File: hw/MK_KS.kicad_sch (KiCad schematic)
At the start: 40 parts, among them J10 Screw_Terminal_01x02, J11 TRS-JACK-KP, J3 KEY_SND_IF, J8 Conn_Coaxial_Power, J9 Screw_Terminal_01x02, Q1 G01N20LE, U4 LM393ADR, U5 Sounder

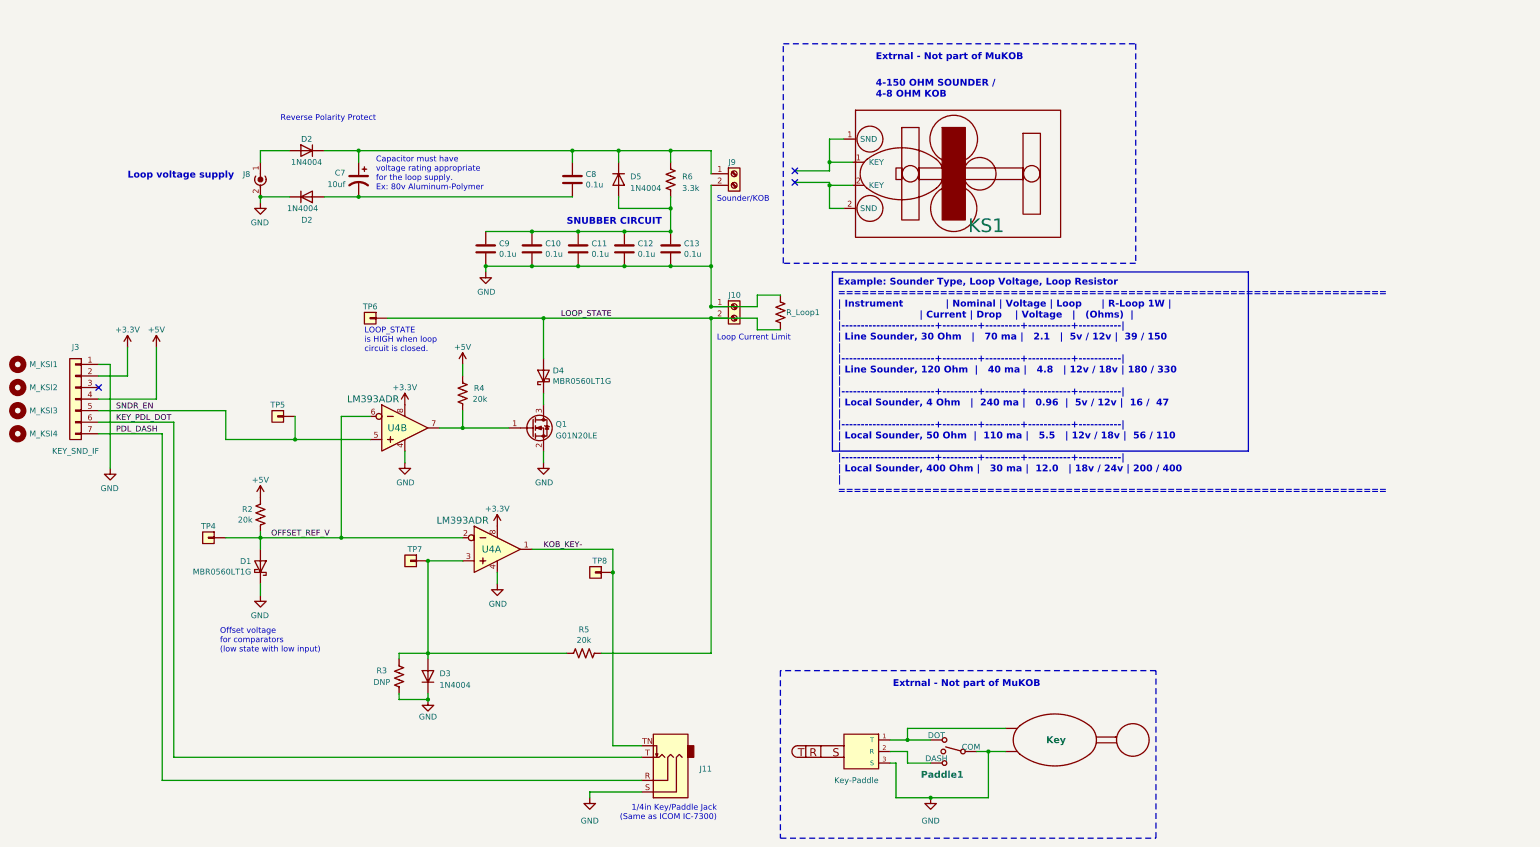
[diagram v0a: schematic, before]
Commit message: Reorganize onto 3 boards. Use 20pin UI connector.
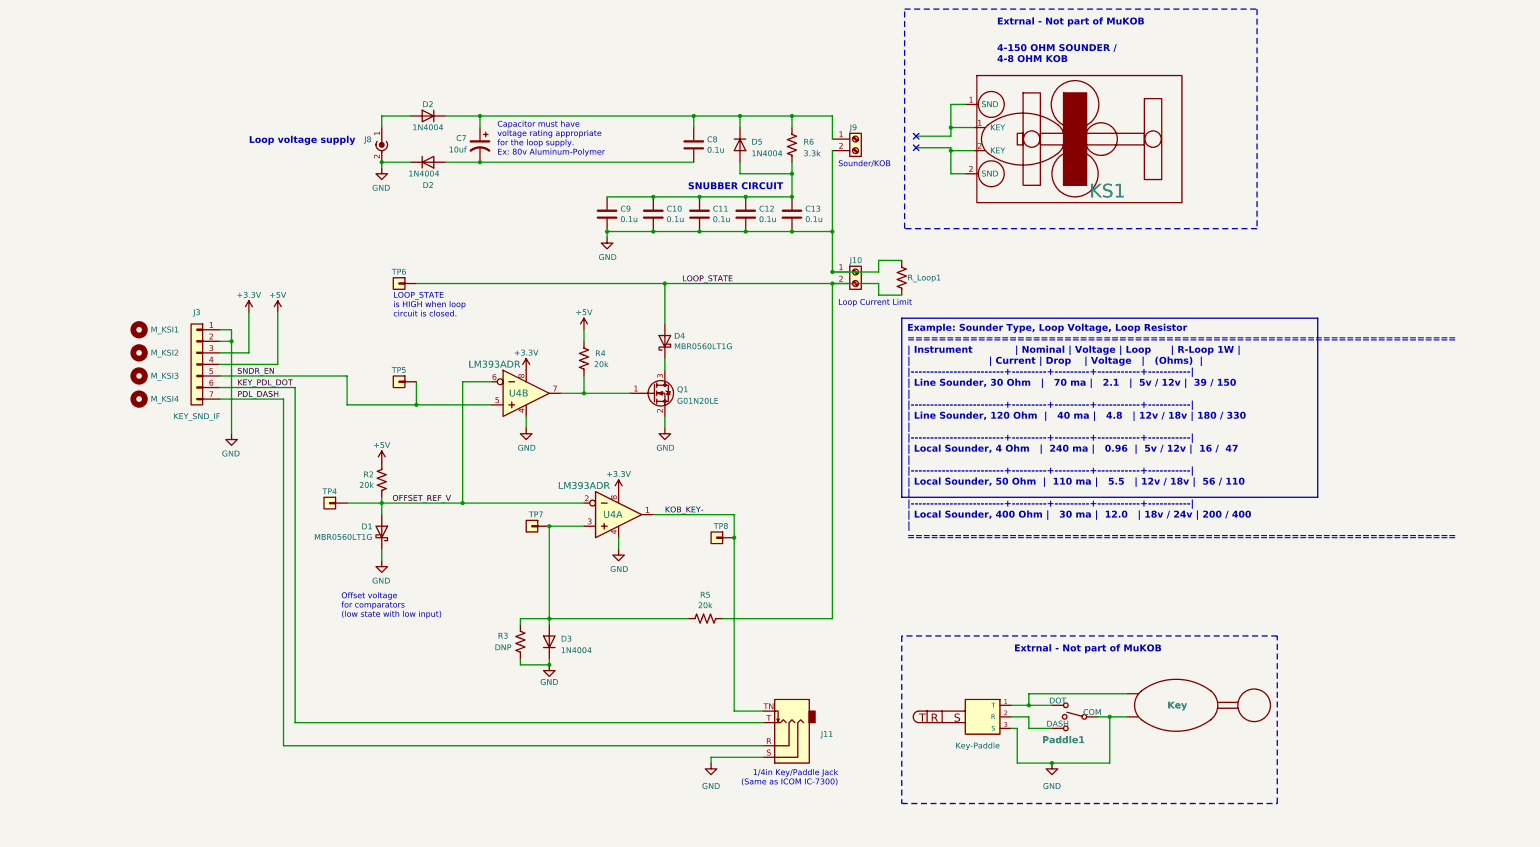
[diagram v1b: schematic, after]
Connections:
- net +3.3V: now also J3.3 (Pin_3); no longer J3.2 (Pin_2)
- net GND: now also J3.2 (Pin_2)
- no-connect marks 3 -> 2
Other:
- note removed: "Reverse Polarity Protect"
- moved on the sheet: C10, C11, C12, C13, C7, C8, C9, D1, D2, D3, D4, D5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

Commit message: Electrical checks complete.
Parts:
- removed M_KSI1, M_KSI2, M_KSI3, M_KSI4: MountingHole, MountingHole:MountingHole_2.7mm_M2.5, symbol Mechanical:MountingHole
- added C9 (x2): 1uF, Capacitor_SMD:C_1206_3216Metric_Pad1.33x1.80mm_HandSolder, symbol Device:C
- added D1: MBR0560LT1G, Diode_SMD:D_SOD-123, symbol Diode:MBR0560
- added D7: 1N4148W, Diode_SMD:D_SOD-123, symbol Diode:1N4148W
- added J4: MKOB-Serial, symbol Connector:DE9_Receptacle_MountingHoles
- added J5: USB_OTG, symbol Connector:USB_OTG
- added JP1, JP2: 1x2 Header, symbol Jumper:Jumper_2_Open
- added LED1: SNDR, LED_THT:LED_D5.0mm, symbol Device:LED
- added M_KSI1, M_KSI2, M_KSI3, M_KSI4, SHLD-1, SHLD-2, SHLD-3, SHLD-4: MountingHole_Pad, symbol Mechanical:MountingHole_Pad
- added Q1 (x2): 2N3904, Package_TO_SOT_THT:TO-92_Inline, symbol Transistor_BJT:2N3904
- added Q8: 2N3905, Package_TO_SOT_THT:TO-92_Inline, symbol Transistor_BJT:2N3905
- added R2: 1k, Resistor_SMD:R_1206_3216Metric_Pad1.30x1.75mm_HandSolder, symbol Device:R_US
- added R2: 100, Resistor_SMD:R_1206_3216Metric_Pad1.30x1.75mm_HandSolder, symbol Device:R_US
- added R5: 10k, Resistor_SMD:R_1206_3216Metric_Pad1.30x1.75mm_HandSolder, symbol Device:R_US
- added R6: 1k, Resistor_THT:R_Axial_DIN0207_L6.3mm_D2.5mm_P10.16mm_Horizontal, symbol Device:R_Small_US
- added R7: 270, Resistor_THT:R_Axial_DIN0207_L6.3mm_D2.5mm_P10.16mm_Horizontal, symbol Device:R_Small_US
- added SW1: KEY/DOT-SW, Button_Switch_SMD:SW_Push_1P1T_NO_Vertical_Wuerth_434133025816, symbol Switch:SW_Push
- added SW1: CLOSER-SW, symbol Switch:SW_SPST
- added SW1: DASH-SW, Button_Switch_SMD:SW_Push_1P1T_NO_Vertical_Wuerth_434133025816, symbol Switch:SW_Push
- added U2: LM358, symbol Amplifier_Operational:LM358
- added U3: MCP1702T-3302E, Package_TO_SOT_SMD:SOT-23, symbol Regulator_Linear:MCP1700x-330xxTT
- D2, D3, D5: footprint Diode_SMD:D_SMB_Handsoldering -> Diode_THT:D_DO-41_SOD81_P10.16mm_Horizontal
- R_Loop1: now left out of the parts list
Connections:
- net +3.3V: now also JP1.2 (B), Q8.1 (E), R6.1
- net +5V: now also C9.1, D1.1 (K), JP2.1 (A), R2.1, U3.3 (VI)
- net GND: now also C7.2, C8.2, D2.2 (A), C9.2, C9.2, D7.2 (A), J4.0 (PAD), J4.5, J5.5 (GND), J5.6 (Shield), M_KSI1.1, M_KSI2.1, M_KSI3.1, M_KSI4.1, Q1.1 (E), R7.2, SHLD-1.1, SHLD-2.1, SHLD-3.1, SHLD-4.1, SW1.1, SW1.1, SW1.1 (A), U3.1 (GND); no longer D2.1 (K), J8.2 (Ext), R_Loop1.1
- net KEY_PDL_DOT: now also SW1.2, SW1.2 (B), U2.3 (+)
- net LOOP_STATE: no longer R_Loop1.2
- net OFFSET_REF_V: now also U2.2 (-), U2.6 (-)
- net PDL_DASH: now also SW1.2, U2.5 (+)
- net SNDR_EN: now also Q8.3 (C), R2.1
- net at C7.1, C8.1, D2.1 (K)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: now also JP2.2 (B)
- new net: D2.1 (K), J8.2 (Ext)
- new net: Q1.1 (E), R7.1
- new net: Q1.3 (C), Q8.2 (B), R6.2
- new net: C9.1, JP1.1 (A), U3.2 (VO)
- new net: LED1.1 (K), Q1.3 (C)
- new net: LED1.2 (A), R2.2
- new net: D1.2 (A), J5.1 (VBUS)
- new net: Q1.2 (B), R2.2
- new net CTS: J4.8, U2.7
- new net DCD: J4.1
- new net DSR: J4.6, U2.1
- new net DTR: J4.4, U2.8 (V+)
- new net LOOP_ENGZ: D7.1 (K), Q1.2 (B), R5.1
- new net RI: J4.9
- new net RTS: J4.7, R5.2
- new net RXD: J4.2
- new net TXD: J4.3, U2.4 (V-)
- no-connect marks 2 -> 8
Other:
- note added: "For Metal Shield"
- note added: "KOB Debug Power DO NOT CONNECT w/Loop Powered"
- note added: "Key/Paddle - Sounder DEBUG Insert 'dummy' in J2 to use dot/dash"
- note added: "MorseKOB/MKOB Interface (optional) DO NOT CONNECT J3 WHEN IN USE"
- note added: "MorseKOB/MKOB Interface Power DO NOT CONNECT for MuKOB"
- note added: "USB Power for MorseKOB/MKOB Interface DO NOT USE for MuKOB"
- moved on the sheet: C10, C11, C12, C13, C7, C8, C9, D1, D2, D3, D4, D5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

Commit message: KeySounder schematic ready for PCB layout.
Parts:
- removed JP2: 1x2 Header, symbol Jumper:Jumper_2_Open
- added JP1: Conn_01x02, symbol Connector_Generic:Conn_01x02
- added OP6: OP_A-B, Connector_PinHeader_1.00mm:PinHeader_1x03_P1.00mm_Vertical, symbol MuKOB:Option_A-B
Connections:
- net +5V: now also JP1.1 (Pin_1), OP6.1 (A); no longer C9.1, U3.3 (VI)
- net LOOP_PWR: now reaches C7.1, C8.1, D2.1 (K), D5.1 (K), J9.1 (Pin_1), R6.1
- net LOOP_PWR: now also JP1.2 (Pin_2), OP6.3 (B)
- new net: C9.1, OP6.2 (C), U3.3 (VI)
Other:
- moved on the sheet: D1, J5

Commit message: Schematic updates. Reorg components between boards. 20 pin ribbon.
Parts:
- removed J-SP1: Key-Paddle, symbol Audio-Plug-TRS:SP-TRS
- removed J11: TRS-JACK-KP, symbol Connector_Audio:AudioJack3_SwitchT
- removed KEY-EXT1: Key, symbol rpikobhat-rescue:Key-Telegraph
- removed Paddle1: PDL_EXT, symbol Switch:SW_SPDT_MSM
- added JP2: 1x2 Header, Connector_PinHeader_2.54mm:PinHeader_1x02_P2.54mm_Vertical, symbol Jumper:Jumper_2_Open
- J3: renamed from J4; footprint (none) -> Connector_Dsub:DSUB-9_Female_Horizontal_P2.77x2.84mm_EdgePinOffset9.90mm_Housed_MountingHolesOffset11.32mm
- J4: renamed from J3; footprint (none) -> Connector_PinSocket_2.54mm:PinSocket_1x07_P2.54mm_Vertical
- JP1: footprint (none) -> Connector_PinHeader_2.54mm:PinHeader_1x02_P2.54mm_Vertical
- JP1: value Conn_01x02 -> LoopDbgPwr; footprint (none) -> Connector_PinHeader_2.54mm:PinHeader_1x02_P2.54mm_Vertical
- OP6: value OP_A-B -> 5V-SRC; footprint Connector_PinHeader_1.00mm:PinHeader_1x03_P1.00mm_Vertical -> Connector_PinHeader_2.54mm:PinHeader_1x03_P2.54mm_Vertical
- TP4, TP5, TP6, TP7, TP8: footprint (none) -> Connector_PinHeader_2.54mm:PinHeader_1x01_P2.54mm_Vertical
- renumbered D7 to D8, J5 to J1, U3 to U1, U2 to U3
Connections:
- net KOB_KEY-: now also JP2.2 (B)
- net KEY_PDL_DOT renamed KEY-
- net KEY-: now also JP2.1 (A)
- net PDL_DASH renamed PDL_DASH-
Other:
- note added: "Key/Paddle - Sounder DEBUG Remove JP2 to use."
- note added: "Normally connected. Remove to use the 'Test Key/Closer'"
- note removed: "1/4in Key/Paddle Jack (Same as ICOM IC-7300)"
- note removed: "Key/Paddle - Sounder DEBUG Insert 'dummy' in J2 to use dot/dash"

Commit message: UI PCB initial
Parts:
- D2, D3, D5: value 1N4004 -> 1N4148; footprint Diode_THT:D_DO-41_SOD81_P10.16mm_Horizontal -> Diode_SMD:D_SOD-123
- D6: renamed from D8; value 1N4148W -> 1N4148
- J1: footprint (none) -> AES_Library:USB_Micro-B_Amphenol_10103594-0001LF_Horizontal_modified
- M_KSI1, M_KSI2, M_KSI3, M_KSI4: footprint (none) -> MountingHole:MountingHole_3.2mm_M3_ISO7380
- SHLD-1, SHLD-2, SHLD-3, SHLD-4: footprint (none) -> MountingHole:MountingHole_4.3mm_M4_ISO14580_Pad_TopBottom
- SW1: footprint (none) -> AES_Library:SW-TGL-Micro-DPST-CIT
- U3: footprint (none) -> Package_SO:SOIC-8_3.9x4.9mm_P1.27mm
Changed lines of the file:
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@@
       (project "MK_KS"
         (path "/c58d90c2-85f3-4e69-91d5-1bcb030f2211"
-          (reference "D6") (unit 1)
+          (reference "D8") (unit 1)
         )
       )
@@
       (effects (font (size 1.27 1.27)) (justify left))
     )
-    (property "Footprint" "" (at 73.66 213.36 0)
+    (property "Footprint" "AES_Library:SW-TGL-Micro-DPST-CIT" (at 73.66 213.36 0)
       (effects (font (size 1.27 1.27)) hide)
     )
@@
       (effects (font (size 1.27 1.27)) (justify left) hide)
     )
-    (property "Footprint" "" (at 400.05 213.36 0)
+    (property "Footprint" "MountingHole:MountingHole_4.3mm_M4_ISO14580_Pad_TopBottom" (at 400.05 213.36 0)
       (effects (font (size 1.27 1.27)) hide)
     )
@@
       (effects (font (size 1.27 1.27)))
     )
-    (property "Footprint" "" (at 36.83 49.53 0)
+    (property "Footprint" "AES_Library:USB_Micro-B_Amphenol_10103594-0001LF_Horizontal_modified" (at 36.83 49.53 0)
       (effects (font (size 1.27 1.27)) hide)
     )
@@
       (effects (font (size 1.27 1.27)) (justify left) hide)
     )
-    (property "Footprint" "" (at 29.21 163.83 0)
+    (property "Footprint" "MountingHole:MountingHole_3.2mm_M3_ISO7380" (at 29.21 163.83 0)
       (effects (font (size 1.27 1.27)) hide)
     )
@@
       (effects (font (size 1.27 1.27)) (justify left) hide)
     )
-    (property "Footprint" "" (at 400.05 208.28 0)
+    (property "Footprint" "MountingHole:MountingHole_4.3mm_M4_ISO14580_Pad_TopBottom" (at 400.05 208.28 0)
       (effects (font (size 1.27 1.27)) hide)
     )
@@
       (effects (font (size 1.27 1.27)) (justify left) hide)
     )
-    (property "Footprint" "" (at 29.21 173.99 0)
+    (property "Footprint" "MountingHole:MountingHole_3.2mm_M3_ISO7380" (at 29.21 173.99 0)
       (effects (font (size 1.27 1.27)) hide)
     )
@@
   (symbol (lib_id "Diode:1N4148W") (at 86.36 109.22 270) (unit 1)
     (in_bom yes) (on_board yes) (dnp no)
-    (property "Reference" "D8" (at 81.28 106.68 90)
-      (effects (font (size 1.27 1.27)) (justify left))
-    )
-    (property "Value" "1N4148W" (at 74.93 109.22 90)
+    (property "Reference" "D6" (at 81.28 106.68 90)
+      (effects (font (size 1.27 1.27)) (justify left))
+    )
+    (property "Value" "1N4148" (at 74.93 109.22 90)
       (effects (font (size 1.27 1.27)) (justify left))
     )
@@
       (project "MK_KS"
         (path "/c58d90c2-85f3-4e69-91d5-1bcb030f2211"
-          (reference "D8") (unit 1)
+          (reference "D6") (unit 1)
         )
       )
@@
       (effects (font (size 1.27 1.27)) (justify right))
     )
-    (property "Value" "1N4004" (at 151.13 67.31 0)
+    (property "Value" "1N4148" (at 151.13 67.31 0)
       (effects (font (size 1.27 1.27)) (justify right))
     )
-    (property "Footprint" "Diode_THT:D_DO-41_SOD81_P10.16mm_Horizontal" (at 148.59 60.325 0)
+    (property "Footprint" "Diode_SMD:D_SOD-123" (at 148.59 60.325 0)
       (effects (font (size 1.27 1.27)) hide)
     )
@@
       (effects (font (size 1.27 1.27)) (justify left) hide)
     )
-    (property "Footprint" "" (at 400.05 218.44 0)
+    (property "Footprint" "MountingHole:MountingHole_4.3mm_M4_ISO14580_Pad_TopBottom" (at 400.05 218.44 0)
       (effects (font (size 1.27 1.27)) hide)
     )
@@
       (effects (font (size 1.27 1.27)) (justify left) hide)
     )
-    (property "Footprint" "" (at 29.21 179.07 0)
+    (property "Footprint" "MountingHole:MountingHole_3.2mm_M3_ISO7380" (at 29.21 179.07 0)
       (effects (font (size 1.27 1.27)) hide)
     )
@@
       (effects (font (size 1.27 1.27)))
     )
-    (property "Value" "1N4004" (at 148.59 57.15 0)
-      (effects (font (size 1.27 1.27)))
-    )
-    (property "Footprint" "Diode_THT:D_DO-41_SOD81_P10.16mm_Horizontal" (at 148.59 59.055 0)
+    (property "Value" "1N4148" (at 148.59 57.15 0)
+      (effects (font (size 1.27 1.27)))
+    )
+    (property "Footprint" "Diode_SMD:D_SOD-123" (at 148.59 59.055 0)
       (effects (font (size 1.27 1.27)) hide)
     )
@@
       (effects (font (size 1.27 1.27)))
     )
-    (property "Footprint" "" (at 80.01 142.24 0)
+    (property "Footprint" "Package_SO:SOIC-8_3.9x4.9mm_P1.27mm" (at 80.01 142.24 0)
       (effects (font (size 1.27 1.27)) hide)
     )
@@
       (effects (font (size 1.27 1.27)) (justify left) hide)
     )
-    (property "Footprint" "" (at 29.21 168.91 0)
+    (property "Footprint" "MountingHole:MountingHole_3.2mm_M3_ISO7380" (at 29.21 168.91 0)
       (effects (font (size 1.27 1.27)) hide)
     )
@@
       (effects (font (size 1.27 1.27)) (justify right) hide)
     )
-    (property "Footprint" "" (at 76.2 74.93 0)
+    (property "Footprint" "Package_SO:SOIC-8_3.9x4.9mm_P1.27mm" (at 76.2 74.93 0)
       (effects (font (size 1.27 1.27)) hide)
     )
@@
       (effects (font (size 1.27 1.27)) (justify right))
     )
-    (property "Value" "1N4004" (at 170.18 227.965 90)
+    (property "Value" "1N4148" (at 170.18 227.965 90)
       (effects (font (size 1.27 1.27)) (justify right))
     )
-    (property "Footprint" "Diode_THT:D_DO-41_SOD81_P10.16mm_Horizontal" (at 172.085 226.06 0)
+    (property "Footprint" "Diode_SMD:D_SOD-123" (at 172.085 226.06 0)
       (effects (font (size 1.27 1.27)) hide)
     )
@@
       (effects (font (size 1.27 1.27)) (justify left) hide)
     )
-    (property "Footprint" "" (at 400.05 223.52 0)
+    (property "Footprint" "MountingHole:MountingHole_4.3mm_M4_ISO14580_Pad_TopBottom" (at 400.05 223.52 0)
       (effects (font (size 1.27 1.27)) hide)
     )
@@
       (effects (font (size 1.27 1.27)))
     )
-    (property "Footprint" "" (at 76.2 74.93 0)
+    (property "Footprint" "Package_SO:SOIC-8_3.9x4.9mm_P1.27mm" (at 76.2 74.93 0)
       (effects (font (size 1.27 1.27)) hide)
     )
@@
       (effects (font (size 1.27 1.27)) (justify left))
     )
-    (property "Value" "1N4004" (at 209.55 62.865 90)
-      (effects (font (size 1.27 1.27)) (justify left))
-    )
-    (property "Footprint" "Diode_THT:D_DO-41_SOD81_P10.16mm_Horizontal" (at 202.565 60.96 0)
-      (effects (font (size 1.27 1.27)) hide)
-    )
+    (property "Value" "1N4148" (at 209.55 62.865 90)
+      (effects (font (size 1.27 1.27)) (justify left))
+    )
+    (property "Footprint" "Diode_SMD:D_SOD-123" (at 202.565 60.96 0)
+      (effects (font (size 1.27 1.27)) hide)
+    )
